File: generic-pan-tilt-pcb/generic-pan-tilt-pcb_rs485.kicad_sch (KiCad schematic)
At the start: 8 parts, among them U4 ISO1450DW

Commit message: rename again to generic-pan-tilt
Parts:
- PS1: symbol pan-tilt-pcb:CME0303S3C -> generic-pan-tilt-pcb:CME0303S3C
- U4: symbol pan-tilt-pcb:ISO1450DW -> generic-pan-tilt-pcb:ISO1450DW
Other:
- title: Pan Tilt PCB: RS485 -> Generic Pan Tilt PCB: RS485
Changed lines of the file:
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@@
 	(paper "USLetter")
 	(title_block
-		(title "Pan Tilt PCB: RS485")
+		(title "Generic Pan Tilt PCB: RS485")
 		(date "2024-07-10")
 		(company "Responsive Environments, MIT Media Lab")
@@
 		)
 		(instances
-			(project "pan-tilt-pcb"
+			(project "generic-pan-tilt-pcb"
 				(path "/e3bbbe58-bf8f-42a8-8505-028de8235dc1/98335103-cef0-473f-a7b3-d62ebdf0389c"
 					(reference "#PWR055")
@@
 		)
 		(instances
-			(project "pan-tilt-pcb"
+			(project "generic-pan-tilt-pcb"
 				(path "/e3bbbe58-bf8f-42a8-8505-028de8235dc1/98335103-cef0-473f-a7b3-d62ebdf0389c"
 					(reference "C23")
@@
 		)
 		(instances
-			(project "pan-tilt-pcb"
+			(project "generic-pan-tilt-pcb"
 				(path "/e3bbbe58-bf8f-42a8-8505-028de8235dc1/98335103-cef0-473f-a7b3-d62ebdf0389c"
 					(reference "#PWR054")
@@
 		)
 		(instances
-			(project "pan-tilt-pcb"
+			(project "generic-pan-tilt-pcb"
 				(path "/e3bbbe58-bf8f-42a8-8505-028de8235dc1/98335103-cef0-473f-a7b3-d62ebdf0389c"
 					(reference "C22")
@@
 		)
 		(instances
-			(project "pan-tilt-pcb"
+			(project "generic-pan-tilt-pcb"
 				(path "/e3bbbe58-bf8f-42a8-8505-028de8235dc1/98335103-cef0-473f-a7b3-d62ebdf0389c"
 					(reference "#PWR056")
@@
 	)
 	(symbol
-		(lib_id "pan-tilt-pcb:ISO1450DW")
+		(lib_id "generic-pan-tilt-pcb:ISO1450DW")
 		(at 148.59 110.49 0)
 		(unit 1)
@@
 		)
 		(instances
-			(project "pan-tilt-pcb"
+			(project "generic-pan-tilt-pcb"
 				(path "/e3bbbe58-bf8f-42a8-8505-028de8235dc1/98335103-cef0-473f-a7b3-d62ebdf0389c"
 					(reference "U4")
@@
 	)
 	(symbol
-		(lib_id "pan-tilt-pcb:CME0303S3C")
+		(lib_id "generic-pan-tilt-pcb:CME0303S3C")
 		(at 148.59 34.29 0)
 		(unit 1)
@@
 		)
 		(instances
-			(project "pan-tilt-pcb"
+			(project "generic-pan-tilt-pcb"
 				(path "/e3bbbe58-bf8f-42a8-8505-028de8235dc1/98335103-cef0-473f-a7b3-d62ebdf0389c"
 					(reference "PS1")
@@
 		)
 		(instances
-			(project "pan-tilt-pcb"
+			(project "generic-pan-tilt-pcb"
 				(path "/e3bbbe58-bf8f-42a8-8505-028de8235dc1/98335103-cef0-473f-a7b3-d62ebdf0389c"
 					(reference "C24")
@@
 		)
 		(instances
-			(project "pan-tilt-pcb"
+			(project "generic-pan-tilt-pcb"
 				(path "/e3bbbe58-bf8f-42a8-8505-028de8235dc1/98335103-cef0-473f-a7b3-d62ebdf0389c"
 					(reference "#FLG06")
@@
 		)
 		(instances
-			(project "pan-tilt-pcb"
+			(project "generic-pan-tilt-pcb"
 				(path "/e3bbbe58-bf8f-42a8-8505-028de8235dc1/98335103-cef0-473f-a7b3-d62ebdf0389c"
 					(reference "C25")
@@
 		)
 		(instances
-			(project "pan-tilt-pcb"
+			(project "generic-pan-tilt-pcb"
 				(path "/e3bbbe58-bf8f-42a8-8505-028de8235dc1/98335103-cef0-473f-a7b3-d62ebdf0389c"
 					(reference "C21")
@@
 		)
 		(instances
-			(project "pan-tilt-pcb"
+			(project "generic-pan-tilt-pcb"
 				(path "/e3bbbe58-bf8f-42a8-8505-028de8235dc1/98335103-cef0-473f-a7b3-d62ebdf0389c"
 					(reference "L2")
@@
 		)
 		(instances
-			(project "pan-tilt-pcb"
+			(project "generic-pan-tilt-pcb"
 				(path "/e3bbbe58-bf8f-42a8-8505-028de8235dc1/98335103-cef0-473f-a7b3-d62ebdf0389c"
 					(reference "#PWR058")
@@
 		)
 		(instances
-			(project "pan-tilt-pcb"
+			(project "generic-pan-tilt-pcb"
 				(path "/e3bbbe58-bf8f-42a8-8505-028de8235dc1/98335103-cef0-473f-a7b3-d62ebdf0389c"
 					(reference "#PWR057")
@@
 		)
 		(instances
-			(project "pan-tilt-pcb"
+			(project "generic-pan-tilt-pcb"
 				(path "/e3bbbe58-bf8f-42a8-8505-028de8235dc1/98335103-cef0-473f-a7b3-d62ebdf0389c"
 					(reference "#PWR059")

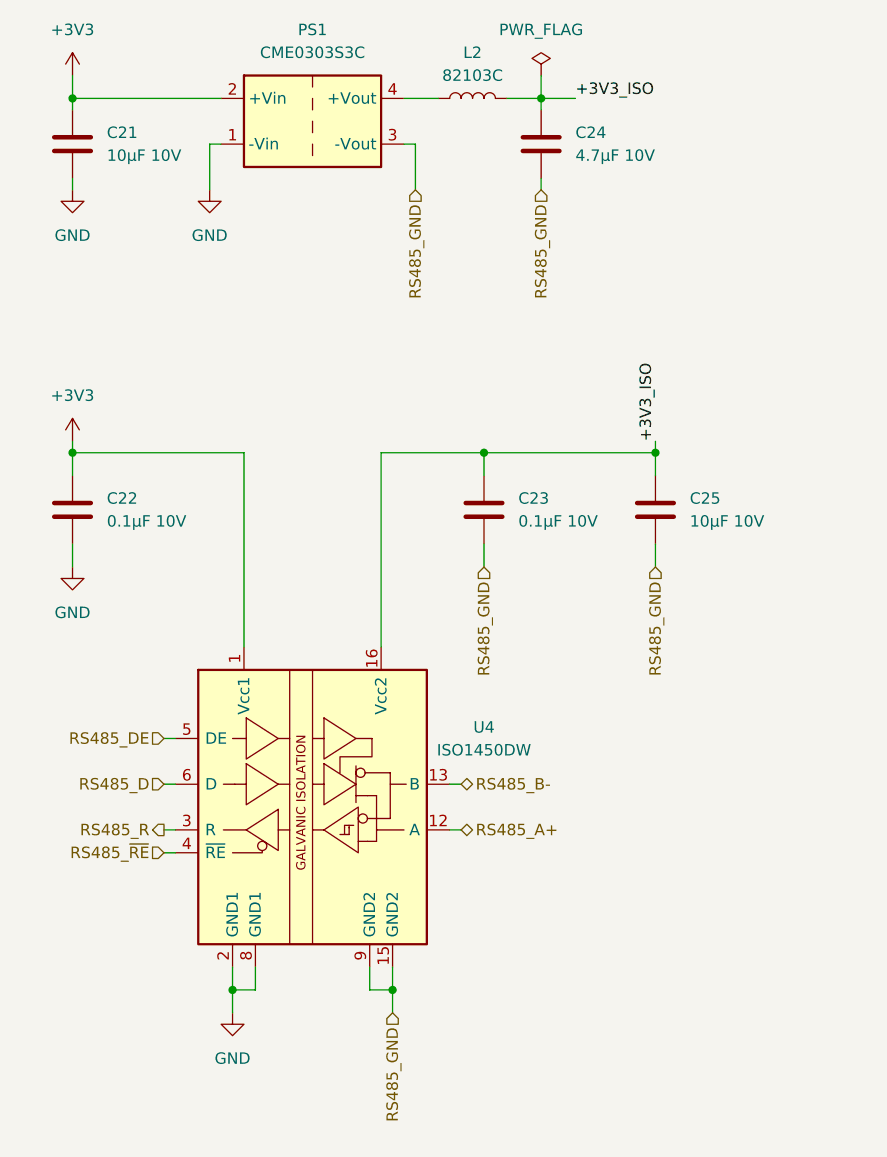
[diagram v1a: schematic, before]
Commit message: pick all footprints, begin layout
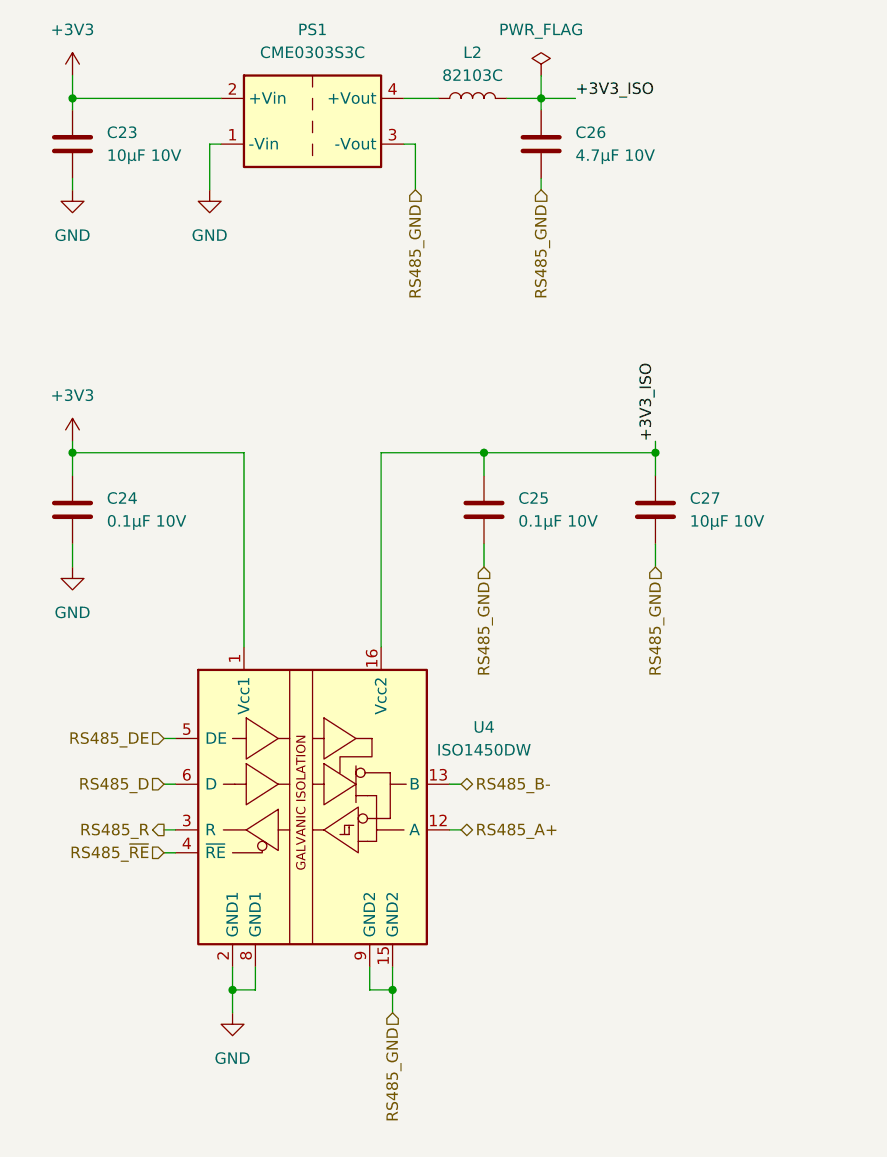
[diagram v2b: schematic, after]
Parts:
- C23: renamed from C21; footprint (none) -> Capacitor_SMD:C_0603_1608Metric
- C24: renamed from C22; footprint (none) -> Capacitor_SMD:C_0603_1608Metric
- C25: renamed from C23; footprint (none) -> Capacitor_SMD:C_0603_1608Metric
- C26: renamed from C24; footprint (none) -> Capacitor_SMD:C_0603_1608Metric
- C27: renamed from C25; footprint (none) -> Capacitor_SMD:C_0603_1608Metric
- L2: footprint (none) -> Inductor_SMD:L_1210_3225Metric
- PS1: footprint Converter_DCDC:Converter_DCDC_Murata_MEE1SxxxxSC_THT -> generic-pan-tilt-pcb:Converter_DCDC_Murata_CMExxxxS3C_THT
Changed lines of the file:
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@@
 		(dnp no)
 		(fields_autoplaced yes)
-		(property "Reference" "#PWR055"
+		(property "Reference" "#PWR054"
 			(at 121.92 48.26 0)
 			(effects
@@
 			(project "generic-pan-tilt-pcb"
 				(path "/e3bbbe58-bf8f-42a8-8505-028de8235dc1/98335103-cef0-473f-a7b3-d62ebdf0389c"
-					(reference "#PWR055")
+					(reference "#PWR054")
 					(unit 1)
 				)
@@
 		(dnp no)
 		(fields_autoplaced yes)
-		(property "Reference" "C23"
+		(property "Reference" "C25"
 			(at 171.45 76.1999 0)
 			(effects
@@
 			)
 		)
-		(property "Footprint" ""
+		(property "Footprint" "Capacitor_SMD:C_0603_1608Metric"
 			(at 168.6052 81.28 0)
 			(effects
@@
 			(project "generic-pan-tilt-pcb"
 				(path "/e3bbbe58-bf8f-42a8-8505-028de8235dc1/98335103-cef0-473f-a7b3-d62ebdf0389c"
-					(reference "C23")
+					(reference "C25")
 					(unit 1)
 				)
@@
 		(dnp no)
 		(fields_autoplaced yes)
-		(property "Reference" "#PWR054"
+		(property "Reference" "#PWR053"
 			(at 121.92 33.02 0)
 			(effects
@@
 			(project "generic-pan-tilt-pcb"
 				(path "/e3bbbe58-bf8f-42a8-8505-028de8235dc1/98335103-cef0-473f-a7b3-d62ebdf0389c"
-					(reference "#PWR054")
+					(reference "#PWR053")
 					(unit 1)
 				)
@@
 		(dnp no)
 		(fields_autoplaced yes)
-		(property "Reference" "C22"
+		(property "Reference" "C24"
 			(at 125.73 76.1999 0)
 			(effects
@@
 			)
 		)
-		(property "Footprint" ""
+		(property "Footprint" "Capacitor_SMD:C_0603_1608Metric"
 			(at 122.8852 81.28 0)
 			(effects
@@
 			(project "generic-pan-tilt-pcb"
 				(path "/e3bbbe58-bf8f-42a8-8505-028de8235dc1/98335103-cef0-473f-a7b3-d62ebdf0389c"
-					(reference "C22")
+					(reference "C24")
 					(unit 1)
 				)
@@
 		(dnp no)
 		(fields_autoplaced yes)
-		(property "Reference" "#PWR056"
+		(property "Reference" "#PWR055"
 			(at 121.92 73.66 0)
 			(effects
@@
 			(project "generic-pan-tilt-pcb"
 				(path "/e3bbbe58-bf8f-42a8-8505-028de8235dc1/98335103-cef0-473f-a7b3-d62ebdf0389c"
-					(reference "#PWR056")
+					(reference "#PWR055")
 					(unit 1)
 				)
@@
 			)
 		)
-		(property "Footprint" "Converter_DCDC:Converter_DCDC_Murata_MEE1SxxxxSC_THT"
+		(property "Footprint" "generic-pan-tilt-pcb:Converter_DCDC_Murata_CMExxxxS3C_THT"
 			(at 121.92 40.64 0)
 			(effects
@@
 			)
 		)
-		(property "Datasheet" "https://www.mouser.com/datasheet/2/281/1/kdc_cme-2941013.pdf"
+		(property "Datasheet" "https://power.murata.com/pub/data/power/ncl/kdc_cme.pdf"
 			(at 175.26 41.91 0)
 			(effects
@@
 		(dnp no)
 		(fields_autoplaced yes)
-		(property "Reference" "C24"
+		(property "Reference" "C26"
 			(at 177.8 35.5599 0)
 			(effects
@@
 			)
 		)
-		(property "Footprint" ""
+		(property "Footprint" "Capacitor_SMD:C_0603_1608Metric"
 			(at 174.9552 40.64 0)
 			(effects
@@
 			(project "generic-pan-tilt-pcb"
 				(path "/e3bbbe58-bf8f-42a8-8505-028de8235dc1/98335103-cef0-473f-a7b3-d62ebdf0389c"
-					(reference "C24")
+					(reference "C26")
 					(unit 1)
 				)
@@
 		(dnp no)
 		(fields_autoplaced yes)
-		(property "Reference" "#FLG06"
+		(property "Reference" "#FLG05"
 			(at 173.99 27.305 0)
 			(effects
@@
 			(project "generic-pan-tilt-pcb"
 				(path "/e3bbbe58-bf8f-42a8-8505-028de8235dc1/98335103-cef0-473f-a7b3-d62ebdf0389c"
-					(reference "#FLG06")
+					(reference "#FLG05")
 					(unit 1)
 				)
@@
 		(dnp no)
 		(fields_autoplaced yes)
-		(property "Reference" "C25"
+		(property "Reference" "C27"
 			(at 190.5 76.1999 0)
 			(effects
@@
 			)
 		)
-		(property "Footprint" ""
+		(property "Footprint" "Capacitor_SMD:C_0603_1608Metric"
 			(at 187.6552 81.28 0)
 			(effects
@@
 			(project "generic-pan-tilt-pcb"
 				(path "/e3bbbe58-bf8f-42a8-8505-028de8235dc1/98335103-cef0-473f-a7b3-d62ebdf0389c"
-					(reference "C25")
+					(reference "C27")
 					(unit 1)
 				)
@@
 		(dnp no)
 		(fields_autoplaced yes)
-		(property "Reference" "C21"
+		(property "Reference" "C23"
 			(at 125.73 35.5599 0)
 			(effects
@@
 			)
 		)
-		(property "Footprint" ""
+		(property "Footprint" "Capacitor_SMD:C_0603_1608Metric"
 			(at 122.8852 40.64 0)
 			(effects
@@
 			(project "generic-pan-tilt-pcb"
 				(path "/e3bbbe58-bf8f-42a8-8505-028de8235dc1/98335103-cef0-473f-a7b3-d62ebdf0389c"
-					(reference "C21")
+					(reference "C23")
 					(unit 1)
 				)
@@
 			)
 		)
-		(property "Footprint" ""
+		(property "Footprint" "Inductor_SMD:L_1210_3225Metric"
 			(at 166.37 31.75 0)
 			(effects
@@
 		(dnp no)
 		(fields_autoplaced yes)
-		(property "Reference" "#PWR058"
+		(property "Reference" "#PWR057"
 			(at 137.16 48.26 0)
 			(effects
@@
 			(project "generic-pan-tilt-pcb"
 				(path "/e3bbbe58-bf8f-42a8-8505-028de8235dc1/98335103-cef0-473f-a7b3-d62ebdf0389c"
-					(reference "#PWR058")
+					(reference "#PWR057")
 					(unit 1)
 				)
@@
 		(dnp no)
 		(fields_autoplaced yes)
-		(property "Reference" "#PWR057"
+		(property "Reference" "#PWR056"
 			(at 121.92 90.17 0)
 			(effects
@@
 			(project "generic-pan-tilt-pcb"
 				(path "/e3bbbe58-bf8f-42a8-8505-028de8235dc1/98335103-cef0-473f-a7b3-d62ebdf0389c"
-					(reference "#PWR057")
+					(reference "#PWR056")
 					(unit 1)
 				)
@@
 		(dnp no)
 		(fields_autoplaced yes)
-		(property "Reference" "#PWR059"
+		(property "Reference" "#PWR058"
 			(at 139.7 139.7 0)
 			(effects
@@
 			(project "generic-pan-tilt-pcb"
 				(path "/e3bbbe58-bf8f-42a8-8505-028de8235dc1/98335103-cef0-473f-a7b3-d62ebdf0389c"
-					(reference "#PWR059")
-					(unit 1)
-				)
+					(reference "#PWR058")
+					(unit 1)
+				)

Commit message: layout progress
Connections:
- net +3V3_ISO_UNFILTERED: now reaches L2.1, PS1.4 (+Vout)
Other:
- moved on the sheet: C26, L2
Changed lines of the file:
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@@
 	)
 	(junction
-		(at 173.99 31.75)
+		(at 194.31 31.75)
 		(diameter 0)
 		(color 0 0 0 0)
@@
 	(wire
 		(pts
-			(xy 173.99 41.91) (xy 173.99 40.64)
+			(xy 194.31 41.91) (xy 194.31 40.64)
 		)
 		(stroke
@@
 	(wire
 		(pts
-			(xy 162.56 31.75) (xy 158.75 31.75)
-		)
-		(stroke
-			(width 0)
-			(type default)
-		)
-	)
-	(wire
-		(pts
-			(xy 173.99 29.21) (xy 173.99 31.75)
+			(xy 182.88 31.75) (xy 158.75 31.75)
+		)
+		(stroke
+			(width 0)
+			(type default)
+		)
+	)
+	(wire
+		(pts
+			(xy 194.31 29.21) (xy 194.31 31.75)
 		)
 		(stroke
@@
 	(wire
 		(pts
-			(xy 177.8 31.75) (xy 173.99 31.75)
+			(xy 198.12 31.75) (xy 194.31 31.75)
 		)
 		(stroke
@@
 	(wire
 		(pts
-			(xy 173.99 33.02) (xy 173.99 31.75)
+			(xy 194.31 33.02) (xy 194.31 31.75)
 		)
 		(stroke
@@
 	(wire
 		(pts
-			(xy 173.99 31.75) (xy 170.18 31.75)
+			(xy 194.31 31.75) (xy 190.5 31.75)
 		)
 		(stroke
@@
 	)
 	(label "+3V3_ISO"
-		(at 177.8 31.75 0)
+		(at 198.12 31.75 0)
 		(fields_autoplaced yes)
 		(effects
@@
 		)
 	)
-	(label "+3V3_ISO"
-		(at 186.69 69.85 90)
+	(label "+3V3_ISO_UNFILTERED"
+		(at 160.02 31.75 0)
 		(fields_autoplaced yes)
 		(effects
@@
 		)
 	)
+	(label "+3V3_ISO"
+		(at 186.69 69.85 90)
+		(fields_autoplaced yes)
+		(effects
+			(font
+				(size 1.27 1.27)
+			)
+			(justify left bottom)
+		)
+	)
 	(hierarchical_label "RS485_GND"
 		(shape input)
-		(at 173.99 41.91 270)
+		(at 194.31 41.91 270)
 		(fields_autoplaced yes)
 		(effects
@@
 	(symbol
 		(lib_id "Device:C")
-		(at 173.99 36.83 0)
+		(at 194.31 36.83 0)
 		(unit 1)
 		(exclude_from_sim no)
@@
 		(fields_autoplaced yes)
 		(property "Reference" "C26"
-			(at 177.8 35.5599 0)
+			(at 198.12 35.5599 0)
 			(effects
 				(font
@@
 		)
 		(property "Value" "4.7μF 10V"
-			(at 177.8 38.0999 0)
+			(at 198.12 38.0999 0)
 			(effects
 				(font
@@
 		)
 		(property "Footprint" "Capacitor_SMD:C_0603_1608Metric"
-			(at 174.9552 40.64 0)
+			(at 195.2752 40.64 0)
 			(effects
 				(font
@@
 		)
 		(property "Datasheet" "~"
-			(at 173.99 36.83 0)
+			(at 194.31 36.83 0)
 			(effects
 				(font
@@
 		)
 		(property "Description" "Unpolarized capacitor"
-			(at 173.99 36.83 0)
+			(at 194.31 36.83 0)
 			(effects
 				(font
@@
 	(symbol
 		(lib_id "power:PWR_FLAG")
-		(at 173.99 29.21 0)
+		(at 194.31 29.21 0)
 		(unit 1)
 		(exclude_from_sim no)
@@
 		(fields_autoplaced yes)
 		(property "Reference" "#FLG05"
-			(at 173.99 27.305 0)
+			(at 194.31 27.305 0)
 			(effects
 				(font
@@
 		)
 		(property "Value" "PWR_FLAG"
-			(at 173.99 24.13 0)
+			(at 194.31 24.13 0)
 			(effects
 				(font
@@
 		)
 		(property "Footprint" ""
-			(at 173.99 29.21 0)
+			(at 194.31 29.21 0)
 			(effects
 				(font
@@
 		)
 		(property "Datasheet" "~"
-			(at 173.99 29.21 0)
+			(at 194.31 29.21 0)
 			(effects
 				(font
@@
 		)
 		(property "Description" "Special symbol for telling ERC where power comes from"
-			(at 173.99 29.21 0)
+			(at 194.31 29.21 0)
 			(effects
 				(font
@@
 	(symbol
 		(lib_id "Device:L")
-		(at 166.37 31.75 90)
+		(at 186.69 31.75 90)
 		(unit 1)
 		(exclude_from_sim no)
@@
 		(fields_autoplaced yes)
 		(property "Reference" "L2"
-			(at 166.37 26.67 90)
+			(at 186.69 26.67 90)
 			(effects
 				(font
@@
 		)
 		(property "Value" "82103C"
-			(at 166.37 29.21 90)
+			(at 186.69 29.21 90)
 			(effects
 				(font
@@
 		)
 		(property "Footprint" "Inductor_SMD:L_1210_3225Metric"
-			(at 166.37 31.75 0)
+			(at 186.69 31.75 0)
 			(effects
 				(font
@@
 		)
 		(property "Datasheet" "~"
-			(at 166.37 31.75 0)
+			(at 186.69 31.75 0)
 			(effects
 				(font
@@
 		)
 		(property "Description" "Inductor"
-			(at 166.37 31.75 0)
-			(effects
-				(font
+			(at 186.69 31.75 0)
+			(effects
+				(font

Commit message: more progress
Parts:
- renumbered C27 to C26, C26 to C27
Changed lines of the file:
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@@
 		(dnp no)
 		(fields_autoplaced yes)
-		(property "Reference" "C26"
+		(property "Reference" "C27"
 			(at 198.12 35.5599 0)
 			(effects
@@
 			(project "generic-pan-tilt-pcb"
 				(path "/e3bbbe58-bf8f-42a8-8505-028de8235dc1/98335103-cef0-473f-a7b3-d62ebdf0389c"
-					(reference "C26")
+					(reference "C27")
 					(unit 1)
 				)
@@
 		(dnp no)
 		(fields_autoplaced yes)
-		(property "Reference" "C27"
+		(property "Reference" "C26"
 			(at 190.5 76.1999 0)
 			(effects
@@
 			(project "generic-pan-tilt-pcb"
 				(path "/e3bbbe58-bf8f-42a8-8505-028de8235dc1/98335103-cef0-473f-a7b3-d62ebdf0389c"
-					(reference "C27")
+					(reference "C26")
 					(unit 1)
 				)

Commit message: begin new routing
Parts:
- C23, C24, C25, C26, C27: footprint Capacitor_SMD:C_0603_1608Metric -> Capacitor_SMD:C_0402_1005Metric
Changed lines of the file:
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@@
 			)
 		)
-		(property "Footprint" "Capacitor_SMD:C_0603_1608Metric"
+		(property "Footprint" "Capacitor_SMD:C_0402_1005Metric"
 			(at 168.6052 81.28 0)
 			(effects
@@
 			)
 		)
-		(property "Footprint" "Capacitor_SMD:C_0603_1608Metric"
+		(property "Footprint" "Capacitor_SMD:C_0402_1005Metric"
 			(at 122.8852 81.28 0)
 			(effects
@@
 			)
 		)
-		(property "Footprint" "Capacitor_SMD:C_0603_1608Metric"
+		(property "Footprint" "Capacitor_SMD:C_0402_1005Metric"
 			(at 195.2752 40.64 0)
 			(effects
@@
 			)
 		)
-		(property "Footprint" "Capacitor_SMD:C_0603_1608Metric"
+		(property "Footprint" "Capacitor_SMD:C_0402_1005Metric"
 			(at 187.6552 81.28 0)
 			(effects
@@
 			)
 		)
-		(property "Footprint" "Capacitor_SMD:C_0603_1608Metric"
+		(property "Footprint" "Capacitor_SMD:C_0402_1005Metric"
 			(at 122.8852 40.64 0)
 			(effects

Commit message: more pcb, kicost maf digikey mouser
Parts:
- L2: digikey# (none) -> 811-2473-1-ND; manf# (none) -> 82103C; mouser# (none) -> 580-82103C
- PS1: digikey# (none) -> 811-2889-5-ND; manf# (none) -> CME0303S3C; mouser# (none) -> 580-CME0303S3C
- U4: digikey# (none) -> 296-ISO1450DW-ND; manf# (none) -> ISO1450DW; mouser# (none) -> 595-ISO1450DW
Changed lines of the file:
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@@
+			)
+		)
+		(property "digikey#" "296-ISO1450DW-ND"
+			(at 148.59 110.49 0)
+			(effects
+				(font
+					(size 1.27 1.27)
+				)
+				(hide yes)
+			)
+		)
+		(property "manf#" "ISO1450DW"
+			(at 148.59 110.49 0)
+			(effects
+				(font
+					(size 1.27 1.27)
+				)
+				(hide yes)
+			)
+		)
+		(property "mouser#" "595-ISO1450DW"
+			(at 148.59 110.49 0)
+			(effects
+				(font
+					(size 1.27 1.27)
+				)
+				(hide yes)
 			)
 		)
@@
 			)
 		)
+		(property "digikey#" "811-2889-5-ND"
+			(at 148.59 34.29 0)
+			(effects
+				(font
+					(size 1.27 1.27)
+				)
+				(hide yes)
+			)
+		)
+		(property "manf#" "CME0303S3C"
+			(at 148.59 34.29 0)
+			(effects
+				(font
+					(size 1.27 1.27)
+				)
+				(hide yes)
+			)
+		)
+		(property "mouser#" "580-CME0303S3C"
+			(at 148.59 34.29 0)
+			(effects
+				(font
+					(size 1.27 1.27)
+				)
+				(hide yes)
+			)
+		)
 		(pin "4"
 		)
@@
 			(at 186.69 31.75 0)
 			(effects
+				(font
+					(size 1.27 1.27)
+				)
+				(hide yes)
+			)
+		)
+		(property "digikey#" "811-2473-1-ND"
+			(at 186.69 31.75 0)
+			(effects
+				(font
+					(size 1.27 1.27)
+				)
+				(hide yes)
+			)
+		)
+		(property "manf#" "82103C"
+			(at 186.69 31.75 0)
+			(effects
+				(font
+					(size 1.27 1.27)
+				)
+				(hide yes)
+			)
+		)
+		(property "mouser#" "580-82103C"
+			(at 186.69 31.75 0)
+			(effects
